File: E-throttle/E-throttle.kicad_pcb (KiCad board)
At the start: 2 copper layers, 88.9 x 72.4 mm, 39 parts, among them J1 PROG, J2 JTAG, J3 Conn_01x11, J4 Conn_01x11, J5 776087-1, Q1 NMOS, SW1 SW_Push, U1 ESP32-S3-WROOM-1-N16R8, U2 LM317_SOT-223, U3 LM317_SOT-223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

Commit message: Run DRC, generate Gerbers
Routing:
- net /IDLE: track 116.3 -> 110.4 mm
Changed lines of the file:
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@@
 			(plot_on_all_layers_selection 0x0000000_00000000)
 			(disableapertmacros no)
-			(usegerberextensions no)
+			(usegerberextensions yes)
 			(usegerberattributes yes)
-			(usegerberadvancedattributes yes)
-			(creategerberjobfile yes)
+			(usegerberadvancedattributes no)
+			(creategerberjobfile no)
 			(dashed_line_dash_ratio 12.000000)
 			(dashed_line_gap_ratio 3.000000)
@@
 			(plotinvisibletext no)
 			(sketchpadsonfab no)
-			(subtractmaskfromsilk no)
+			(subtractmaskfromsilk yes)
 			(outputformat 1)
 			(mirror no)
-			(drillshape 1)
+			(drillshape 0)
 			(scaleselection 1)
-			(outputdirectory "")
+			(outputdirectory "generated/gerbers/")
 		)
 	)
@@
 		(width 0.2)
 		(layer "B.Cu")
-		(net 57)
-	)
-	(segment
-		(start 165.196 133.16)
-		(end 165.2085 133.1725)
-		(width 0.2)
-		(layer "B.Cu")
-		(net 57)
-	)
-	(segment
-		(start 165.2085 133.1725)
-		(end 165.2085 137.993605)
-		(width 0.2)
-		(layer "B.Cu")
-		(net 57)
-	)
-	(segment
-		(start 165.2085 137.993605)
-		(end 164.428053 138.774052)
-		(width 0.2)
-		(layer "B.Cu")

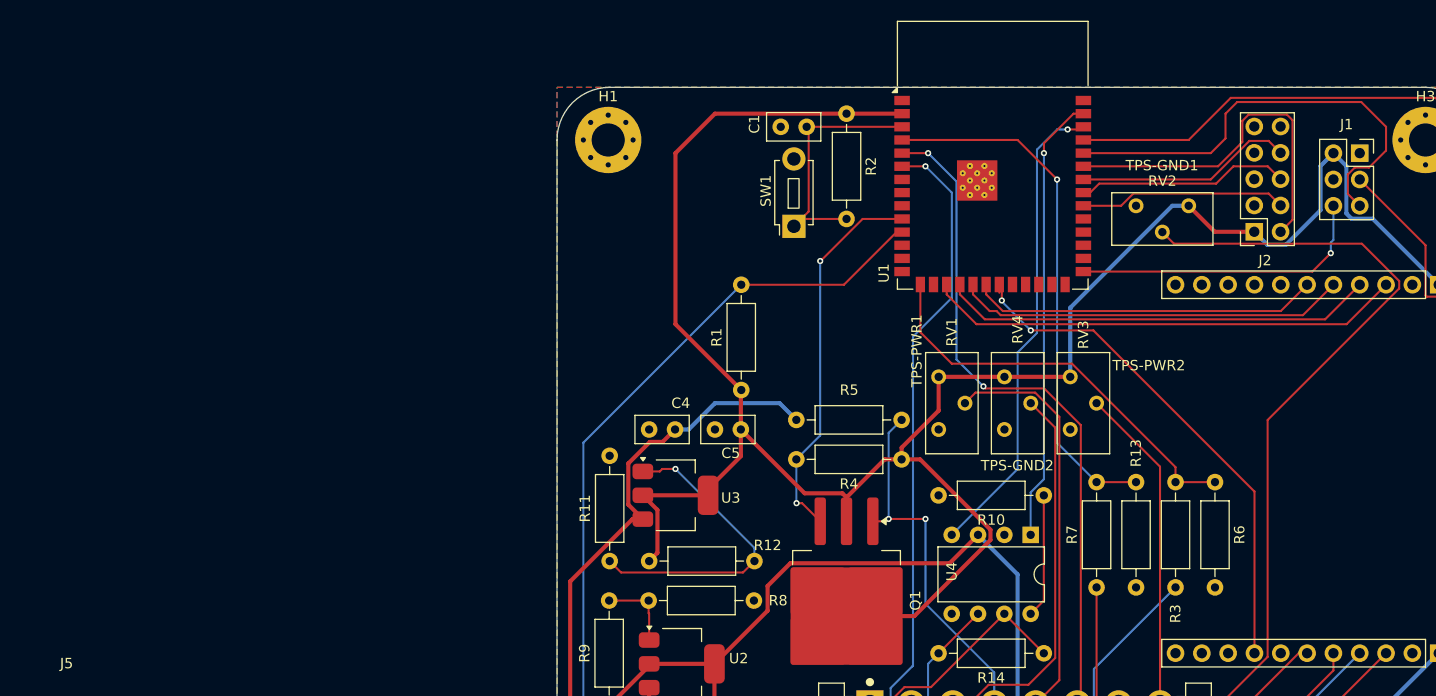
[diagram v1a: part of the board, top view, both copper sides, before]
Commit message: Added relay, added all footprints to schematic
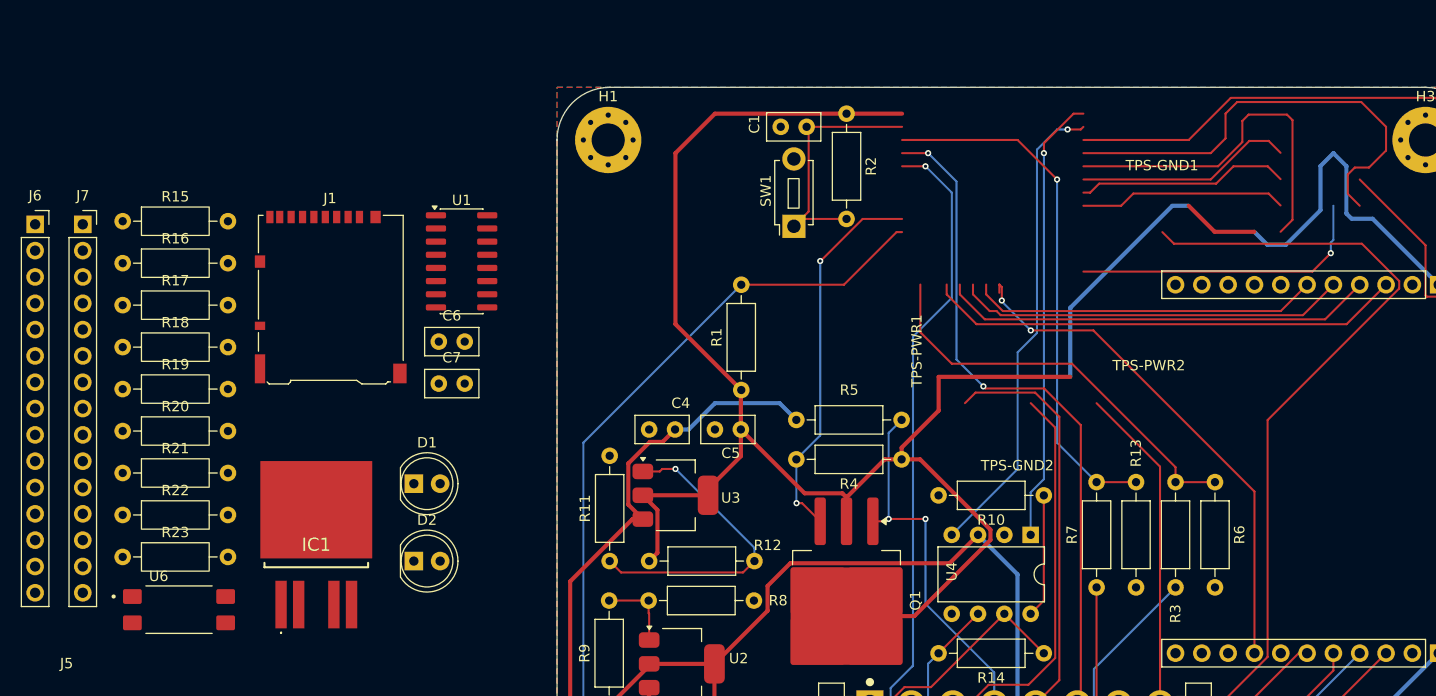
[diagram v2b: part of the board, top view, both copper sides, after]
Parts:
- removed J2: JTAG, Connector_PinSocket_2.54mm:PinSocket_2x05_P2.54mm_Vertical
- removed RV1, RV2, RV3, RV4: 100k, Potentiometer_THT:Potentiometer_Bourns_3296Y_Vertical
- added C6: 1u, Capacitor_THT:C_Disc_D5.0mm_W2.5mm_P2.50mm, F.Cu at (115.6, 98.2)
- added C7: 1u, Capacitor_THT:C_Disc_D5.0mm_W2.5mm_P2.50mm, F.Cu at (115.6, 102.2)
- added D1: LED, LED_THT:LED_D5.0mm, F.Cu at (113.2, 111.9)
- added D2: LED, LED_THT:LED_D5.0mm, F.Cu at (113.2, 119.4)
- added IC1: BTS441TG, BTS441TG_KiCad:BTS441TG, F.Cu at (103.8, 117.2)
- added J6: Conn_01x15, Connector_PinSocket_2.54mm:PinSocket_1x15_P2.54mm_Vertical, F.Cu at (76.6, 86.9)
- added J7: Conn_01x15, Connector_PinSocket_2.54mm:PinSocket_1x15_P2.54mm_Vertical, F.Cu at (81.2, 86.9)
- added R15: 33.2k, Resistor_THT:R_Axial_DIN0207_L6.3mm_D2.5mm_P10.16mm_Horizontal, F.Cu at (85.1, 86.6)
- added R16: 66.5k, Resistor_THT:R_Axial_DIN0207_L6.3mm_D2.5mm_P10.16mm_Horizontal, F.Cu at (85.1, 90.6)
- added R17: 33.2k, Resistor_THT:R_Axial_DIN0207_L6.3mm_D2.5mm_P10.16mm_Horizontal, F.Cu at (85.1, 94.7)
- added R18: 66.5k, Resistor_THT:R_Axial_DIN0207_L6.3mm_D2.5mm_P10.16mm_Horizontal, F.Cu at (85.1, 98.7)
- added R19: 100k, Resistor_THT:R_Axial_DIN0207_L6.3mm_D2.5mm_P10.16mm_Horizontal, F.Cu at (85.1, 102.8)
- added R20: 100k, Resistor_THT:R_Axial_DIN0207_L6.3mm_D2.5mm_P10.16mm_Horizontal, F.Cu at (85.1, 106.8)
- added R21: 10k, Resistor_THT:R_Axial_DIN0207_L6.3mm_D2.5mm_P10.16mm_Horizontal, F.Cu at (85.1, 110.9)
- added R22: 220, Resistor_THT:R_Axial_DIN0207_L6.3mm_D2.5mm_P10.16mm_Horizontal, F.Cu at (85.1, 114.9)
- added R23: 220, Resistor_THT:R_Axial_DIN0207_L6.3mm_D2.5mm_P10.16mm_Horizontal, F.Cu at (85.1, 119.0)
- added U6: TLP241A_TP1_F, TLP241A_TP1_F:SOIC254P1000X425-4N, F.Cu at (90.5, 124.1)
- J1: value PROG -> Micro_SD_Card_Det1; footprint Connector_PinSocket_2.54mm:PinSocket_2x03_P2.54mm_Vertical -> Connector_Card:microSD_HC_Hirose_DM3AT-SF-PEJM5
- U1: value ESP32-S3-WROOM-1-N16R8 -> 74HC123; footprint RF_Module:ESP32-S3-WROOM-1 -> Package_SO:SOIC-16_3.9x9.9mm_P1.27mm
- moved J1 100.3 mm to (105.2, 93.9)
- moved U1 52.3 mm to (117.8, 90.5)
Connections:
- J1 pad 1: /PROG_EN -> unconnected-(J1-DAT2-Pad1)
- J1 pad 2: +3V3 -> /CARD_CS
- J1 pad 3: /UART_TX -> /SPI-MOSI
- J1 pad 4: GND -> +3V3
- J1 pad 5: /UART_RX -> /SPI-SCK
- J1 pad 6: /BOOTOPT -> GND
- J3 pad 3: /SPI-CS -> /MOTOR-CS
- J4 pad 1: +12VStep -> +12VStep-SAFE
- J5 pad 10: /TPS-GND2 -> GND
- J5 pad 15: GND -> /STEP-1+
- J5 pad 16: /CAN-H -> /STEP-1-
- J5 pad 17: /CAN-L -> /STEP-2+
- J5 pad 18: GND -> /STEP-2-
- J5 pad 19: GND -> /CAN-H
- J5 pad 20: /STEP-1+ -> /CAN-L
- J5 pad 21: /STEP-1- -> /RELAY_1
- J5 pad 22: /STEP-2+ -> /RELAY_2
- J5 pad 23: /STEP-2- -> GND
- J5 pad 5: /TPS-PWR1 -> +5V
- J5 pad 7: /TPS-GND1 -> GND
- J5 pad 8: /TPS-PWR2 -> +5V
- U1 pad 10: /BLIP-OUT -> /ESP_HEARTBEAT_L2
- U1 pad 11: /IDLE -> +3V3
- U1 pad 12: unconnected-(U1-IO8-Pad12) -> Net-(D2-A)
- U1 pad 13: unconnected-(U1-IO19-Pad13) -> /WD_ENABLE_STEP_PROFET
- U1 pad 14: unconnected-(U1-IO20-Pad14) -> Net-(U1A-Cext)
- U1 pad 15: /APPS-SIG1-OUT -> Net-(U1A-RCext)
- U1 pad 16: unconnected-(U1-IO46-Pad16) -> (no net)
- U1 pad 2: +3V3 -> /ESP_HEARTBEAT_L1
- U1 pad 3: /ENABLE -> +3V3
- U1 pad 4: /APPS-SIG2-OUT -> Net-(D1-A)
- U1 pad 5: /TPS-SIG1 -> /WD_ENABLE_STEP_RELAY
- U1 pad 6: /TPS-SIG2 -> Net-(U1B-Cext)
- U1 pad 7: unconnected-(U1-IO7-Pad7) -> Net-(U1B-RCext)
- U1 pad 8: unconnected-(U1-IO15-Pad8) -> (no net)
- U1 pad 9: unconnected-(U1-IO16-Pad9) -> GND
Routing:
- net (no net): track 0.00 -> 242.6 mm, vias 0 -> 1
- net GND: track 0.00 -> 125.6 mm
- net /TPS-GND1: track 84.2 -> 0.00 mm
- net /UART_TX: track 72.7 -> 0.00 mm
- net +5V: track 75.5 -> 146.2 mm
- net /SPI-CS: track 46.1 -> 0.00 mm
- net /MOTOR-CS: track 0.00 -> 46.1 mm
- net /UART_RX: track 44.1 -> 0.00 mm
- net /TPS-GND2: track 41.3 -> 0.00 mm
- net /TPS-PWR1: track 39.1 -> 0.00 mm
- net /JTAG_TMS: track 34.9 -> 0.00 mm
- net /TPS-PWR2: track 31.6 -> 0.00 mm
- net /BOOTOPT: track 29.3 -> 0.00 mm, vias 1 -> 0
- net /JTAG_TDI: track 21.0 -> 0.00 mm
- net /JTAG_TDO: track 20.6 -> 0.00 mm
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
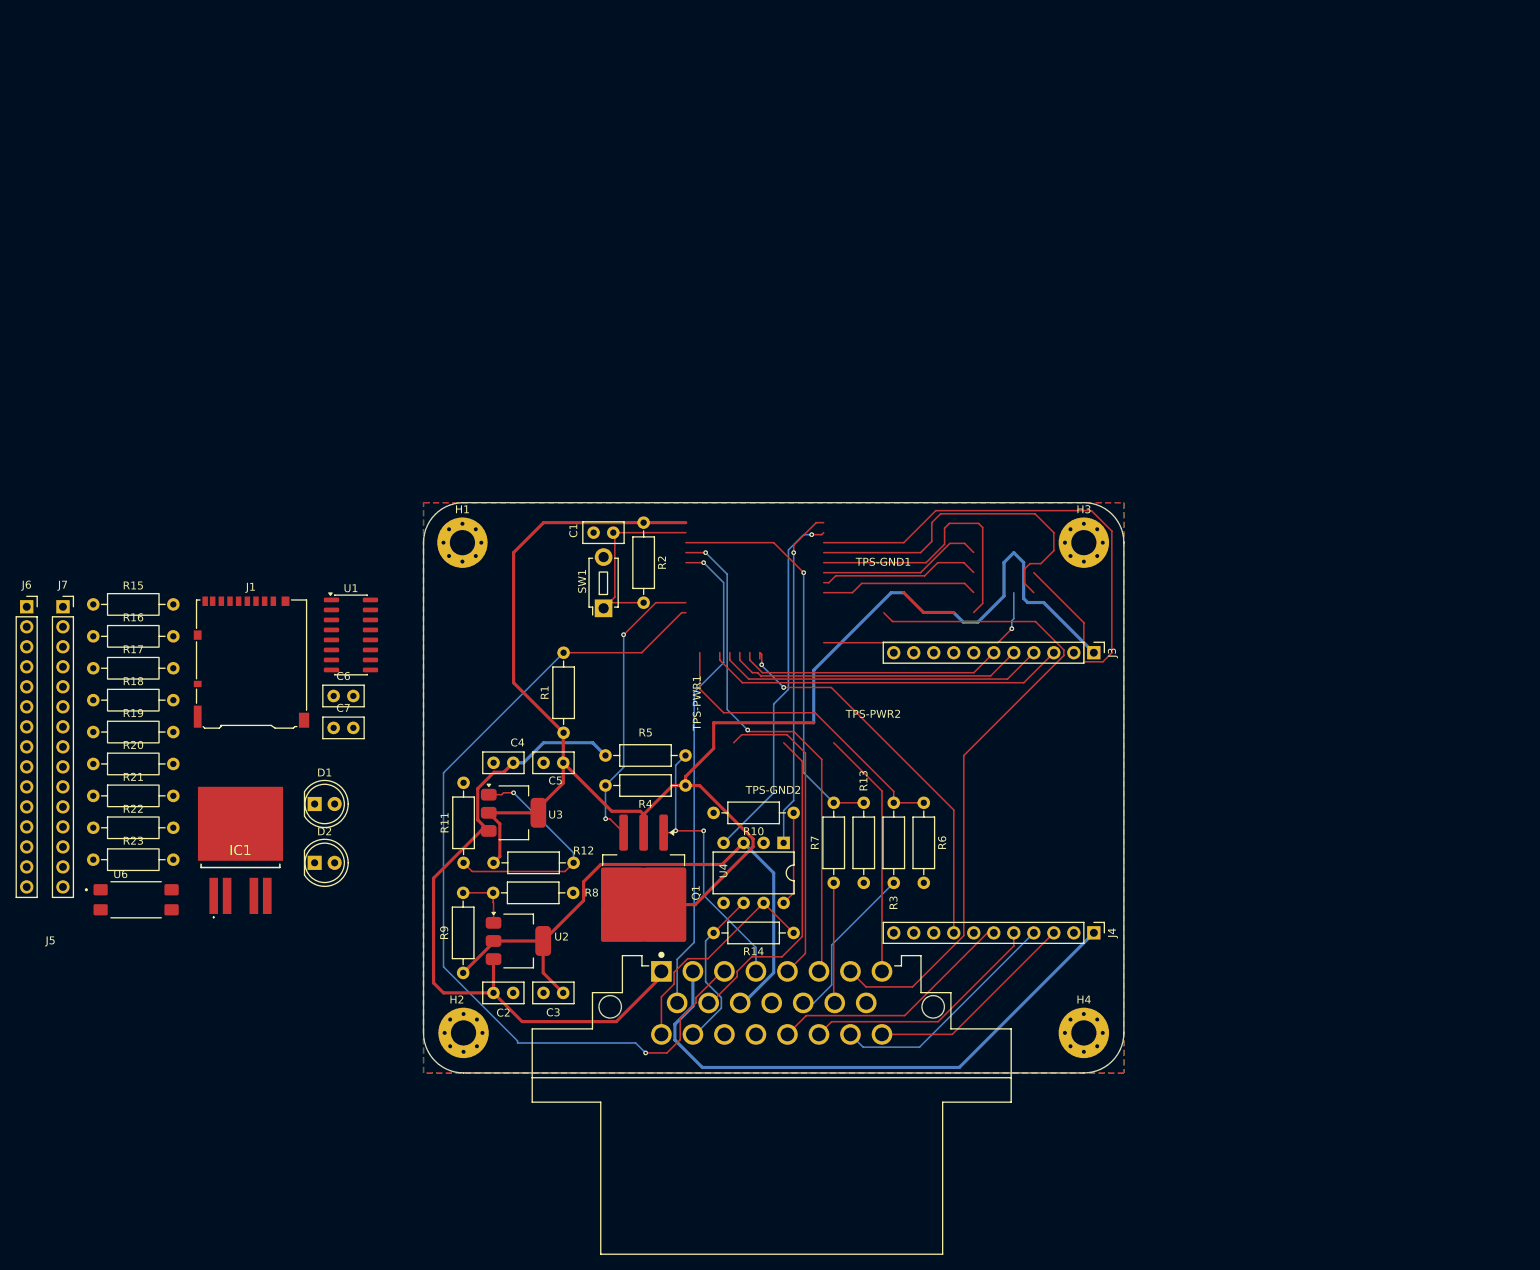
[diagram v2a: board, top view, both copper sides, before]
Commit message: Initial PCB Layout edit
- Added ESP32 Dev Board footprint
- Expanded PCB layout edges
- Added all components in new layout
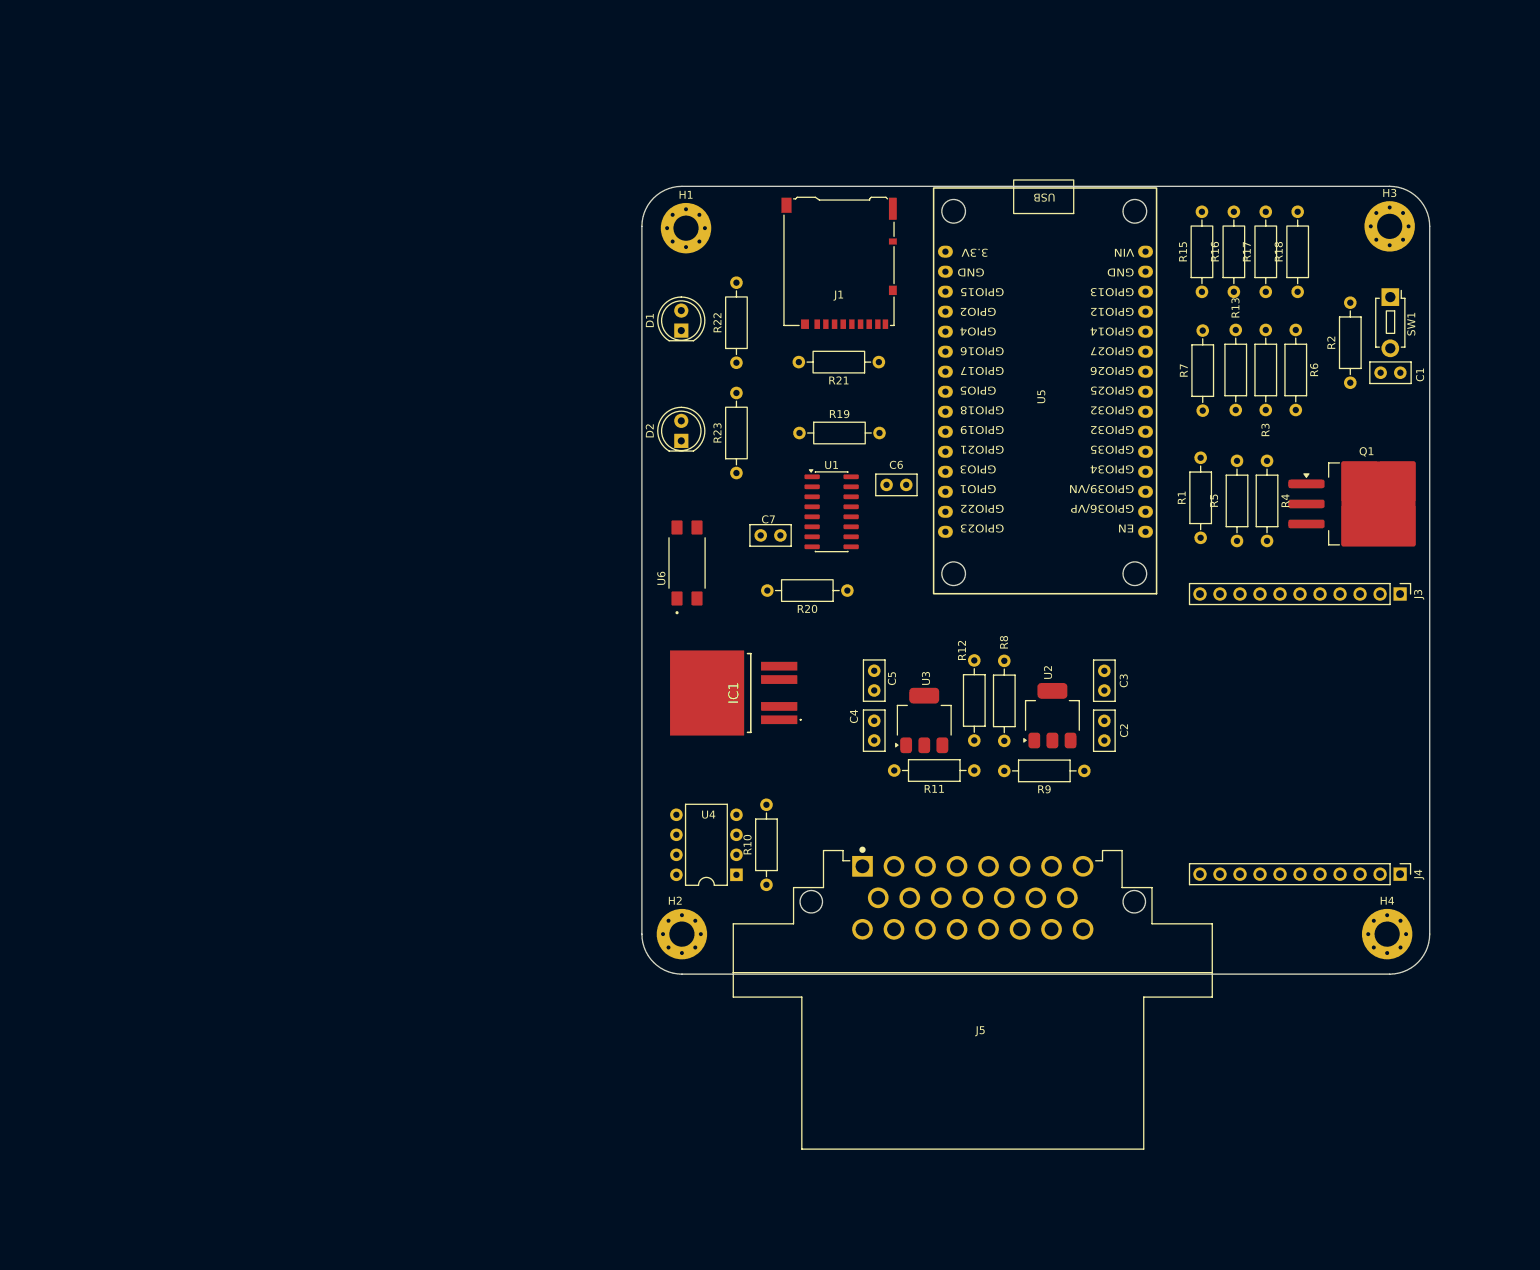
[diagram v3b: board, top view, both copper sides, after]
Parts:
- removed J6, J7: Conn_01x15, Connector_PinSocket_2.54mm:PinSocket_1x15_P2.54mm_Vertical
- removed R14: 120, Resistor_THT:R_Axial_DIN0207_L6.3mm_D2.5mm_P10.16mm_Horizontal
- added U5: ~, FBR_Footprints_additional:ESP32_30pin, F.Cu at (206.7, 58.8)
- moved G*** 191.2 mm to (38.0, 23.5)
- moved R18 161.4 mm to (238.0, 46.9), turned to 90 degrees
- moved R17 156.3 mm to (233.9, 46.9), turned to 90 degrees
- moved R16 151.2 mm to (229.9, 46.9), turned to 90 degrees
- moved R15 146.2 mm to (225.8, 46.9), turned to 90 degrees
- moved R21 113.9 mm to (184.8, 55.8), turned to 180 degrees
- moved SW1 107.4 mm to (249.7, 47.6), turned to -90 degrees
- moved Q1 104.2 mm to (246.7, 73.8), turned to 0 degrees
- moved R22 100.7 mm to (166.7, 55.9), turned to 90 degrees
- moved C1 99.5 mm to (248.5, 57.2), turned to 0 degrees
- moved R20 98.2 mm to (180.8, 84.8), turned to 180 degrees
- moved R19 97.3 mm to (174.7, 64.8)
- moved R23 95.3 mm to (166.7, 69.9), turned to 90 degrees
- moved R2 91.4 mm to (244.6, 58.4), turned to 90 degrees
- moved J1 90.1 mm to (179.8, 43.3), turned to 180 degrees
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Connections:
- net /CARD_DETECT renamed /CARD-DETECT
- J1 pad 2: /CARD_CS -> /CARD-CS
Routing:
- net (no net): track 242.6 -> 0.00 mm, vias 1 -> 0
- net +3V3: track 209.5 -> 0.00 mm
- net +5V: track 146.2 -> 0.00 mm
- net GND: track 125.6 -> 0.00 mm
- net /IDLE: track 110.4 -> 0.00 mm, vias 1 -> 0
- net +12V: track 86.3 -> 0.00 mm
- net +12VStep: track 71.4 -> 0.00 mm
- net /TPS-SIG1: track 65.2 -> 0.00 mm, vias 2 -> 0
- net /TPS-SIG2: track 61.6 -> 0.00 mm, vias 1 -> 0
- net /APPS-SIG2-OUT: track 51.1 -> 0.00 mm, vias 1 -> 0
- net /DIAG0: track 50.1 -> 0.00 mm, vias 2 -> 0
- net /MOTOR-CS: track 46.1 -> 0.00 mm
- net /CAN_RX: track 46.0 -> 0.00 mm, vias 1 -> 0
- net /CAN_TX: track 43.3 -> 0.00 mm, vias 1 -> 0
- net /SPI-SCK: track 41.9 -> 0.00 mm
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- removed copper zone on B.Cu, net GND
- removed copper zone on F.Cu, net GND
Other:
- board size 88.9 x 72.4 mm -> 100 x 100 mm
- board text added: "Designed by Samuel Liu and Clement Tong, Mar 2026"
- board text removed: "Designed by Nonthapat U and Clement Tong, Feb 2025"
- board text removed: "TPS-GND1"
- board text removed: "TPS-GND2"
- board text removed: "TPS-PWR1"
- board text removed: "TPS-PWR2"
